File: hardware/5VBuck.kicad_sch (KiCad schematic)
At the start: 12 parts, among them U10 LMR51635XDDCR

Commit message: update kicad sharepoint
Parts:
- C47: LCSC P/N (none) -> C22387800
- C48: footprint Capacitor_SMD:C_0805_2012Metric_Pad1.18x1.45mm_HandSolder -> Capacitor_SMD:C_0603_1608Metric_Pad1.08x0.95mm_HandSolder; LCSC P/N (none) -> C14663
- C49: LCSC P/N (none) -> C14663
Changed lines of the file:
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@@
 			)
 		)
-		(property "LCSC P/N" ""
+		(property "LCSC P/N" "C22387800"
 			(at 109.22 64.77 0)
 			(hide yes)
@@
 		)
 		(property "P/N" "MSASL168SB5475KTNA01"
+			(at 109.22 64.77 0)
+			(hide yes)
+			(show_name no)
+			(do_not_autoplace no)
+			(effects
+				(font
+					(size 1.27 1.27)
+				)
+			)
+		)
+		(property "LCSC" ""
 			(at 109.22 64.77 0)
 			(hide yes)
@@
 			)
 		)
+		(property "LCSC" ""
+			(at 242.57 106.68 0)
+			(hide yes)
+			(show_name no)
+			(do_not_autoplace no)
+			(effects
+				(font
+					(size 1.27 1.27)
+				)
+			)
+		)
 		(pin "1"
 		)
@@
 			)
 		)
+		(property "LCSC" ""
+			(at 176.53 64.77 90)
+			(hide yes)
+			(show_name no)
+			(do_not_autoplace no)
+			(effects
+				(font
+					(size 1.27 1.27)
+				)
+			)
+		)
 		(pin "1"
 		)
@@
 			)
 		)
+		(property "LCSC" ""
+			(at 255.27 106.68 0)
+			(hide yes)
+			(show_name no)
+			(do_not_autoplace no)
+			(effects
+				(font
+					(size 1.27 1.27)
+				)
+			)
+		)
 		(pin "1"
 		)
@@
 		)
 		(property "Description" "test point"
+			(at 242.57 119.38 0)
+			(hide yes)
+			(show_name no)
+			(do_not_autoplace no)
+			(effects
+				(font
+					(size 1.27 1.27)
+				)
+			)
+		)
+		(property "LCSC" ""
 			(at 242.57 119.38 0)
 			(hide yes)
@@
 			)
 		)
+		(property "LCSC" ""
+			(at 129.54 59.69 0)
+			(hide yes)
+			(show_name no)
+			(do_not_autoplace no)
+			(effects
+				(font
+					(size 1.27 1.27)
+				)
+			)
+		)
 		(pin "2"
 		)
@@
 		)
 		(property "Description" "test point"
+			(at 255.27 119.38 0)
+			(hide yes)
+			(show_name no)
+			(do_not_autoplace no)
+			(effects
+				(font
+					(size 1.27 1.27)
+				)
+			)
+		)
+		(property "LCSC" ""
 			(at 255.27 119.38 0)
 			(hide yes)
@@
 			)
 		)
+		(property "LCSC" ""
+			(at 196.85 68.58 0)
+			(hide yes)
+			(show_name no)
+			(do_not_autoplace no)
+			(effects
+				(font
+					(size 1.27 1.27)
+				)
+			)
+		)
 		(pin "1"
 		)
@@
 			)
 		)
-		(property "LCSC P/N" ""
+		(property "LCSC P/N" "C14663"
+			(at 168.91 62.23 0)
+			(hide yes)
+			(show_name no)
+			(do_not_autoplace no)
+			(effects
+				(font
+					(size 1.27 1.27)
+				)
+			)
+		)
+		(property "LCSC" ""
 			(at 168.91 62.23 0)
 			(hide yes)
@@
 			)
 		)
+		(property "LCSC" ""
+			(at 240.03 64.77 0)
+			(hide yes)
+			(show_name no)
+			(do_not_autoplace no)
+			(effects
+				(font
+					(size 1.27 1.27)
+				)
+			)
+		)
 		(pin "1"
 		)
@@
 			)
 		)
-		(property "Footprint" "Capacitor_SMD:C_0805_2012Metric_Pad1.18x1.45mm_HandSolder"
+		(property "Footprint" "Capacitor_SMD:C_0603_1608Metric_Pad1.08x0.95mm_HandSolder"
 			(at 118.11 67.31 0)
 			(hide yes)
@@
 			)
 		)
-		(property "LCSC P/N" ""
+		(property "LCSC P/N" "C14663"
 			(at 118.11 67.31 0)
 			(hide yes)
@@
 		)
 		(property "P/N" "MLASH168SB7104KTNA01"
+			(at 118.11 67.31 0)
+			(hide yes)
+			(show_name no)
+			(do_not_autoplace no)
+			(effects
+				(font
+					(size 1.27 1.27)
+				)
+			)
+		)
+		(property "LCSC" ""
 			(at 118.11 67.31 0)
 			(hide yes)
@@
 			(at 240.03 72.39 0)
 			(hide yes)
+			(show_name no)
+			(do_not_autoplace no)
+			(effects
+				(font
+					(size 1.27 1.27)
+				)
+			)
+		)
+		(property "LCSC" ""
+			(at 240.03 72.39 0)
+			(hide yes)

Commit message: sorry im omw
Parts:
- removed C50: 47u, Capacitor_SMD:C_1210_3225Metric_Pad1.33x2.70mm_HandSolder, symbol Device:C_Small
- added C47, C48: 22u, Capacitor_SMD:C_1210_3225Metric_Pad1.33x2.70mm_HandSolder, symbol Device:C
- added C49: 3.3u, Capacitor_SMD:C_0805_2012Metric_Pad1.18x1.45mm_HandSolder, symbol Device:C
- C22: renamed from C47; LCSC P/N C22387800 -> C6962403; P/N MSASL168SB5475KTNA01 -> 08055D475KAT4A
- C23: renamed from C48; LCSC P/N C14663 -> C6666325
- C24: renamed from C49; LCSC P/N C14663 -> C6666325
- L1: footprint LHRS_Passives:SRN8040-150M -> LHRS_Passives:74439369082
- R51: footprint Resistor_SMD:R_0603_1608Metric -> Resistor_SMD:R_0603_1608Metric_Pad0.98x0.95mm_HandSolder; LCSC P/N (none) -> C25803; P/N AE1206BR-07100KL -> CRCW0603100KFKEE
- R52: footprint Resistor_SMD:R_0603_1608Metric -> Resistor_SMD:R_0603_1608Metric_Pad0.98x0.95mm_HandSolder; LCSC P/N (none) -> C844132; P/N ERA-2ARB1912X -> CRCW060319K1FKEAHP
- TP21: footprint TestPoint:TestPoint_THTPad_D3.0mm_Drill1.5mm -> TestPoint:TestPoint_Loop_D2.50mm_Drill1.0mm_LowProfile
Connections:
- net GND: now also C47.2, C48.2, C49.2
- net V_out_5V: now also C47.1, C48.1, C49.1
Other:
- moved on the sheet: C22, C23, C24, L1, R51, R52, U10

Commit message: craigenyah
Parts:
- renumbered C22 to C88, C23 to C89, C24 to C90, C47 to C91, C48 to C92, C49 to C93, L1 to L2, R51 to R118, R52 to R119, TP18 to TP45, TP19 to TP46, TP20 to TP47, TP21 to TP48, U10 to U11
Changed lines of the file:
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@@
 		(dnp no)
 		(fields_autoplaced yes)
-		(property "Reference" "C22"
+		(property "Reference" "C88"
 			(at 96.52 59.6962 0)
 			(show_name no)
@@
 			(project "PS-LVCarrier"
 				(path "/9bab2d9d-20f3-40ef-8545-e1299efec47e/194a8848-c0d2-44dd-9e5b-1946509490d6/243ac4a9-8c9a-48d2-8744-855b9f7d516f"
-					(reference "C22")
+					(reference "C88")
 					(unit 1)
 				)
@@
 		(in_pos_files yes)
 		(dnp no)
-		(property "Reference" "TP18"
+		(property "Reference" "TP45"
 			(at 229.87 98.2979 0)
 			(hide yes)
@@
 			(project "PS-LVCarrier"
 				(path "/9bab2d9d-20f3-40ef-8545-e1299efec47e/194a8848-c0d2-44dd-9e5b-1946509490d6/243ac4a9-8c9a-48d2-8744-855b9f7d516f"
-					(reference "TP18")
+					(reference "TP45")
 					(unit 1)
 				)
@@
 		(in_pos_files yes)
 		(dnp no)
-		(property "Reference" "L1"
+		(property "Reference" "L2"
 			(at 161.29 62.484 90)
 			(show_name no)
@@
 			(project "PS-LVCarrier"
 				(path "/9bab2d9d-20f3-40ef-8545-e1299efec47e/194a8848-c0d2-44dd-9e5b-1946509490d6/243ac4a9-8c9a-48d2-8744-855b9f7d516f"
-					(reference "L1")
+					(reference "L2")
 					(unit 1)
 				)
@@
 		(in_pos_files yes)
 		(dnp no)
-		(property "Reference" "TP20"
+		(property "Reference" "TP47"
 			(at 242.57 98.2979 0)
 			(hide yes)
@@
 			(project "PS-LVCarrier"
 				(path "/9bab2d9d-20f3-40ef-8545-e1299efec47e/194a8848-c0d2-44dd-9e5b-1946509490d6/243ac4a9-8c9a-48d2-8744-855b9f7d516f"
-					(reference "TP20")
+					(reference "TP47")
 					(unit 1)
 				)
@@
 		(in_pos_files yes)
 		(dnp no)
-		(property "Reference" "TP19"
+		(property "Reference" "TP46"
 			(at 229.87 110.9979 0)
 			(hide yes)
@@
 			(project "PS-LVCarrier"
 				(path "/9bab2d9d-20f3-40ef-8545-e1299efec47e/194a8848-c0d2-44dd-9e5b-1946509490d6/243ac4a9-8c9a-48d2-8744-855b9f7d516f"
-					(reference "TP19")
+					(reference "TP46")
 					(unit 1)
 				)
@@
 		(dnp no)
 		(fields_autoplaced yes)
-		(property "Reference" "U10"
+		(property "Reference" "U11"
 			(at 129.54 45.72 0)
 			(show_name no)
@@
 			(project "PS-LVCarrier"
 				(path "/9bab2d9d-20f3-40ef-8545-e1299efec47e/194a8848-c0d2-44dd-9e5b-1946509490d6/243ac4a9-8c9a-48d2-8744-855b9f7d516f"
-					(reference "U10")
+					(reference "U11")
 					(unit 1)
 				)
@@
 		(in_pos_files yes)
 		(dnp no)
-		(property "Reference" "TP21"
+		(property "Reference" "TP48"
 			(at 242.57 110.9979 0)
 			(hide yes)
@@
 			(project "PS-LVCarrier"
 				(path "/9bab2d9d-20f3-40ef-8545-e1299efec47e/194a8848-c0d2-44dd-9e5b-1946509490d6/243ac4a9-8c9a-48d2-8744-855b9f7d516f"
-					(reference "TP21")
+					(reference "TP48")
 					(unit 1)
 				)
@@
 		(in_pos_files yes)
 		(dnp no)
-		(property "Reference" "C47"
+		(property "Reference" "C91"
 			(at 164.084 68.58 0)
 			(show_name no)
@@
 			(project "PS-LVCarrier"
 				(path "/9bab2d9d-20f3-40ef-8545-e1299efec47e/194a8848-c0d2-44dd-9e5b-1946509490d6/243ac4a9-8c9a-48d2-8744-855b9f7d516f"
-					(reference "C47")
+					(reference "C91")
 					(unit 1)
 				)
@@
 		(in_pos_files yes)
 		(dnp no)
-		(property "Reference" "C49"
+		(property "Reference" "C93"
 			(at 189.992 68.58 0)
 			(show_name no)
@@
 			(project "PS-LVCarrier"
 				(path "/9bab2d9d-20f3-40ef-8545-e1299efec47e/194a8848-c0d2-44dd-9e5b-1946509490d6/243ac4a9-8c9a-48d2-8744-855b9f7d516f"
-					(reference "C49")
+					(reference "C93")
 					(unit 1)
 				)
@@
 		(in_pos_files yes)
 		(dnp no)
-		(property "Reference" "C24"
+		(property "Reference" "C90"
 			(at 156.718 54.61 0)
 			(show_name no)
@@
 			(project "PS-LVCarrier"
 				(path "/9bab2d9d-20f3-40ef-8545-e1299efec47e/194a8848-c0d2-44dd-9e5b-1946509490d6/243ac4a9-8c9a-48d2-8744-855b9f7d516f"
-					(reference "C24")
+					(reference "C90")
 					(unit 1)
 				)
@@
 		(dnp no)
 		(fields_autoplaced yes)
-		(property "Reference" "R51"
+		(property "Reference" "R118"
 			(at 227.33 59.6899 0)
 			(show_name no)
@@
 			(project "PS-LVCarrier"
 				(path "/9bab2d9d-20f3-40ef-8545-e1299efec47e/194a8848-c0d2-44dd-9e5b-1946509490d6/243ac4a9-8c9a-48d2-8744-855b9f7d516f"
-					(reference "R51")
+					(reference "R118")
 					(unit 1)
 				)
@@
 		(dnp no)
 		(fields_autoplaced yes)
-		(property "Reference" "C23"
+		(property "Reference" "C89"
 			(at 105.41 62.2362 0)
 			(show_name no)
@@
 			(project "PS-LVCarrier"
 				(path "/9bab2d9d-20f3-40ef-8545-e1299efec47e/194a8848-c0d2-44dd-9e5b-1946509490d6/243ac4a9-8c9a-48d2-8744-855b9f7d516f"
-					(reference "C23")
+					(reference "C89")
 					(unit 1)
 				)
@@
 		(dnp no)
 		(fields_autoplaced yes)
-		(property "Reference" "R52"
+		(property "Reference" "R119"
 			(at 227.33 67.3099 0)
 			(show_name no)
@@
 			(project "PS-LVCarrier"
 				(path "/9bab2d9d-20f3-40ef-8545-e1299efec47e/194a8848-c0d2-44dd-9e5b-1946509490d6/243ac4a9-8c9a-48d2-8744-855b9f7d516f"
-					(reference "R52")
+					(reference "R119")
 					(unit 1)
 				)
@@
 		(in_pos_files yes)
 		(dnp no)
-		(property "Reference" "C48"
+		(property "Reference" "C92"
 			(at 173.482 68.834 0)
 			(show_name no)
@@
 			(project "PS-LVCarrier"
 				(path "/9bab2d9d-20f3-40ef-8545-e1299efec47e/194a8848-c0d2-44dd-9e5b-1946509490d6/243ac4a9-8c9a-48d2-8744-855b9f7d516f"
-					(reference "C48")
-					(unit 1)
-				)
+					(reference "C92")
+					(unit 1)
+				)

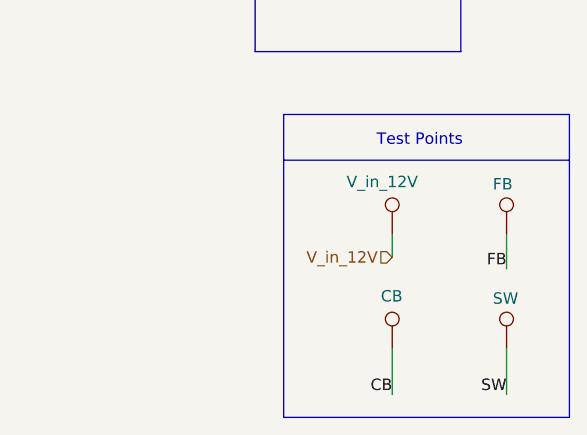
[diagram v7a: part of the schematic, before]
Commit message: switch, stll working
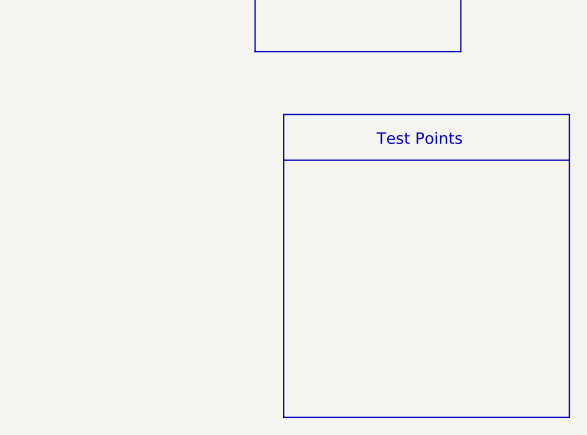
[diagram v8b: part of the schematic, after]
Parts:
- removed TP45: V_in_12V, TestPoint:TestPoint_THTPad_D3.0mm_Drill1.5mm, symbol Connector:TestPoint
- removed TP46: CB, TestPoint:TestPoint_THTPad_D3.0mm_Drill1.5mm, symbol Connector:TestPoint
- removed TP47: FB, TestPoint:TestPoint_THTPad_D3.0mm_Drill1.5mm, symbol Connector:TestPoint
- removed TP48: SW, TestPoint:TestPoint_Loop_D2.50mm_Drill1.0mm_LowProfile, symbol Connector:TestPoint
